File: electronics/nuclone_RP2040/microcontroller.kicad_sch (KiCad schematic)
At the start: 1 part

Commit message: WIP: added schematic component and started defining schematic
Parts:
- added U? (x3): (no value), symbol SquantorRaspberryPi:rp2040
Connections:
- net GPIO_00: now also U?.2 (GPIO0)
- net GPIO_01: now also U?.3 (GPIO1)
- net RESET: now also U?.26 (RUN)
- net TCK: now also U?.24 (SWCLK)
- net TMS: now also U?.25 (SWDIO)
- net VSS: now also U?.19 (TESTEN), U?.57 (GND)
- new net GPIO10: U?.13 (GPIO10)
- new net GPIO11: U?.14 (GPIO11)
- new net GPIO12: U?.15 (GPIO12)
- new net GPIO13: U?.16 (GPIO13)
- new net GPIO14: U?.17 (GPIO14)
- new net GPIO15: U?.18 (GPIO15)
- new net GPIO16: U?.27 (GPIO16)
- new net GPIO2: U?.4 (GPIO2)
- new net GPIO3: U?.5 (GPIO3)
- new net GPIO4: U?.6 (GPIO4)
- new net GPIO5: U?.7 (GPIO5)
- new net GPIO6: U?.8 (GPIO6)
- new net GPIO7: U?.9 (GPIO7)
- new net GPIO8: U?.11 (GPIO8)
- new net GPIO9: U?.12 (GPIO9)
- new net USB_DM: U?.46 (USB_DM)
- new net USB_DP: U?.47 (USB_DP)
- no-connect marks 30 -> 0

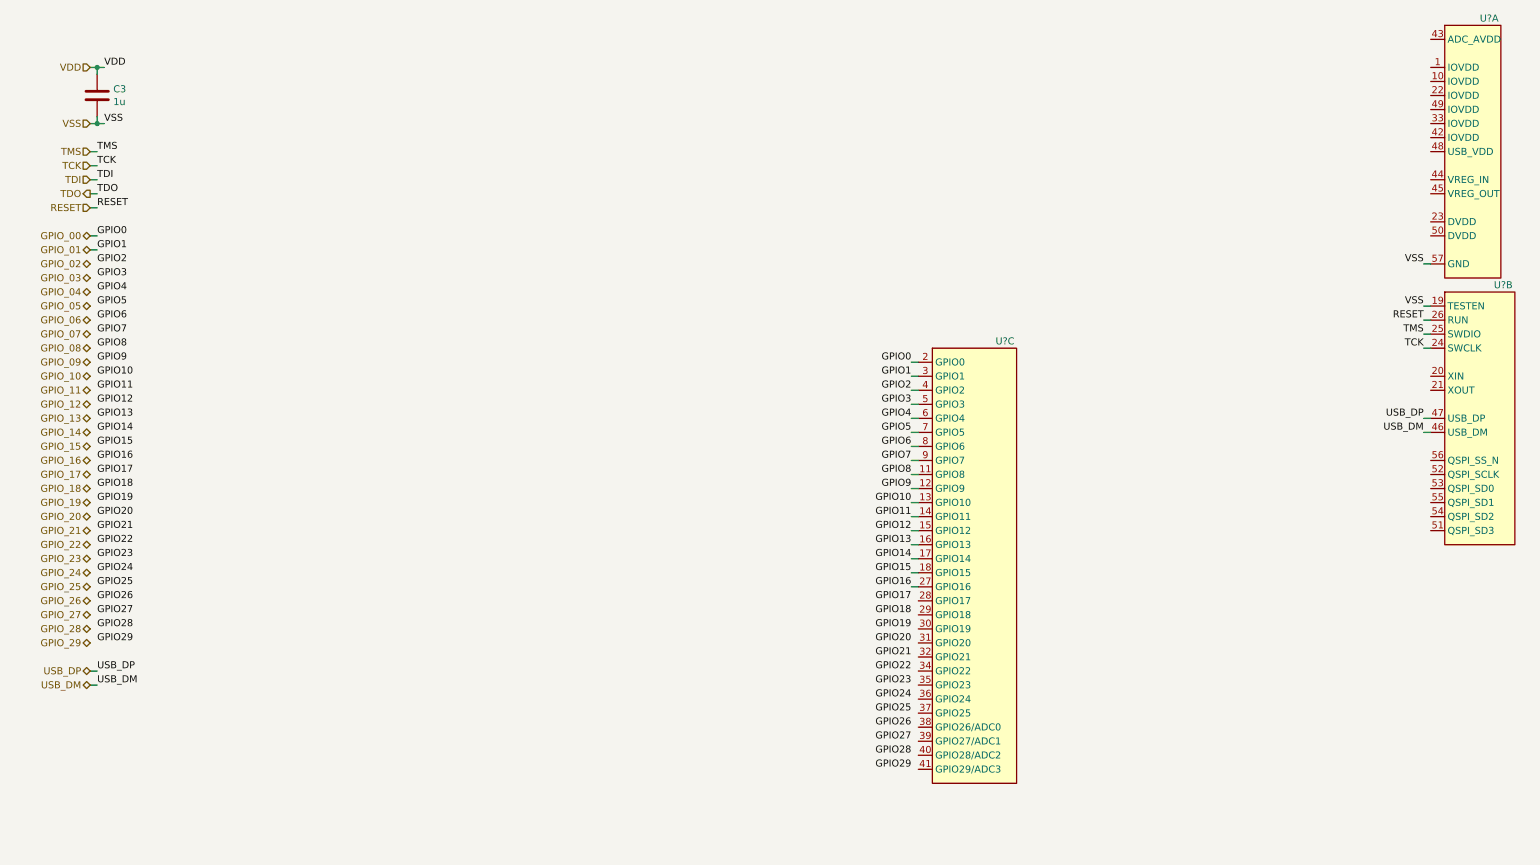
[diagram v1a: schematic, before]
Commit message: WIP rp2040 powersupply schematic part
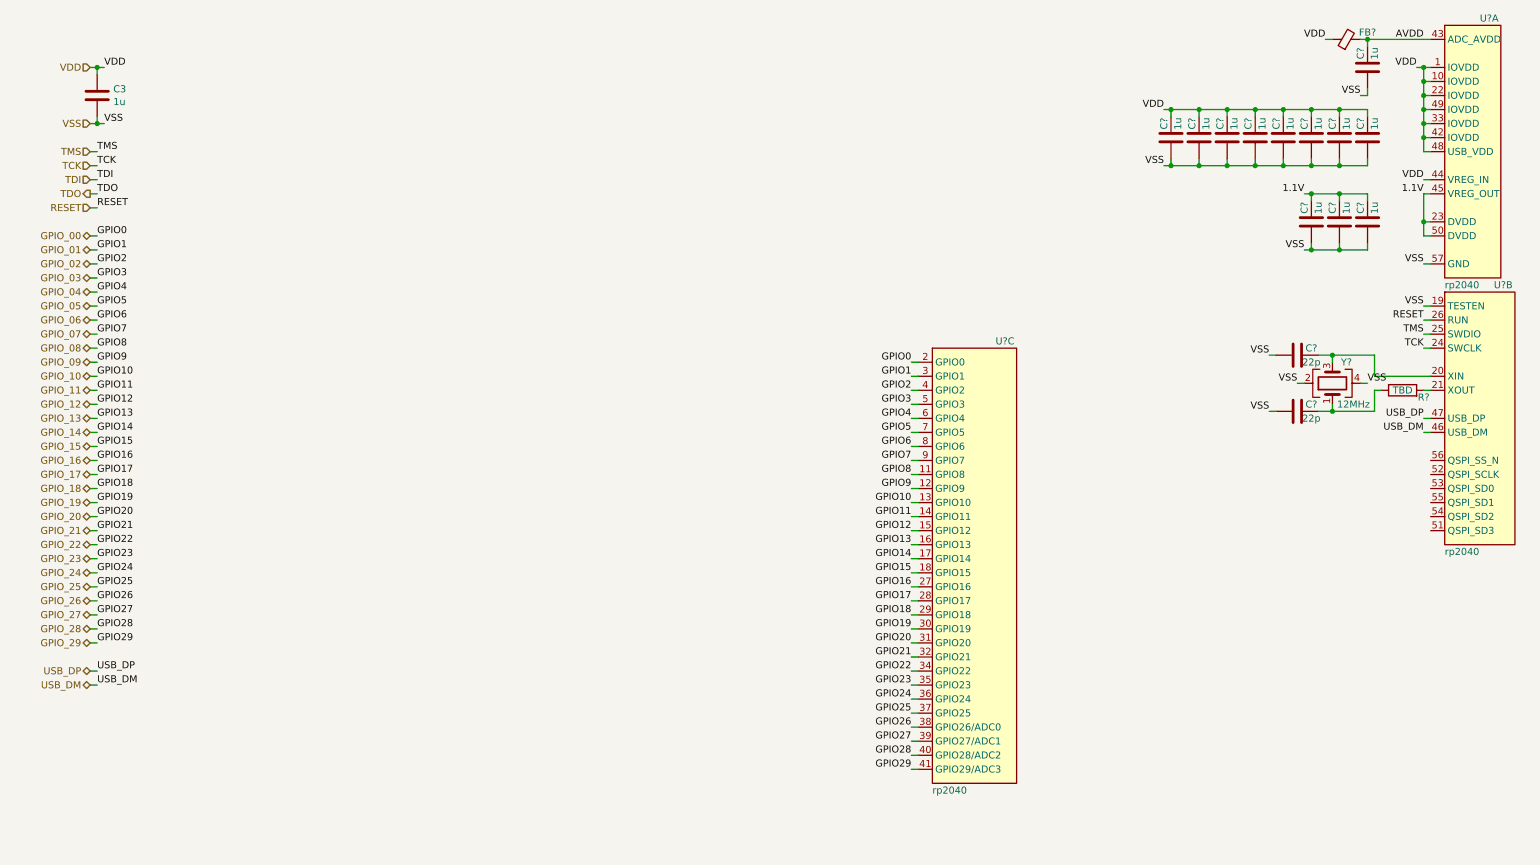
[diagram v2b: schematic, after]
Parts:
- added C? (x12): 1u, SquantorRcl:C_0402, symbol Device:C
- added C? (x2): 22p, SquantorRcl:C_0402, symbol Device:C
- added FB?: (no value), symbol Device:FerriteBead_Small
- added R?: TBD, SquantorRcl:R_0402_hand, symbol Device:R
- added Y?: 12MHz, SquantorCrystal:Crystal_3225_4, symbol Device:Crystal_GND24
- U? (x3): value (none) -> rp2040
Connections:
- net GPIO10 is gone; now on net GPIO_10: U?.13 (GPIO10)
- net GPIO11 is gone; now on net GPIO_11: U?.14 (GPIO11)
- net GPIO12 is gone; now on net GPIO_12: U?.15 (GPIO12)
- net GPIO13 is gone; now on net GPIO_13: U?.16 (GPIO13)
- net GPIO14 is gone; now on net GPIO_14: U?.17 (GPIO14)
- net GPIO15 is gone; now on net GPIO_15: U?.18 (GPIO15)
- net GPIO16 is gone; now on net GPIO_16: U?.27 (GPIO16)
- net GPIO2 is gone; now on net GPIO_02: U?.4 (GPIO2)
- net GPIO3 is gone; now on net GPIO_03: U?.5 (GPIO3)
- net GPIO4 is gone; now on net GPIO_04: U?.6 (GPIO4)
- net GPIO5 is gone; now on net GPIO_05: U?.7 (GPIO5)
- net GPIO6 is gone; now on net GPIO_06: U?.8 (GPIO6)
- net GPIO7 is gone; now on net GPIO_07: U?.9 (GPIO7)
- net GPIO8 is gone; now on net GPIO_08: U?.11 (GPIO8)
- net GPIO9 is gone; now on net GPIO_09: U?.12 (GPIO9)
- net GPIO_17: now also U?.28 (GPIO17)
- net GPIO_18: now also U?.29 (GPIO18)
- net GPIO_19: now also U?.30 (GPIO19)
- net GPIO_20: now also U?.31 (GPIO20)
- net GPIO_21: now also U?.32 (GPIO21)
- net GPIO_22: now also U?.34 (GPIO22)
- net GPIO_23: now also U?.35 (GPIO23)
- net GPIO_24: now also U?.36 (GPIO24)
- net GPIO_25: now also U?.37 (GPIO25)
- net GPIO_26: now also U?.38 (GPIO26/ADC0)
- net GPIO_27: now also U?.39 (GPIO27/ADC1)
- net GPIO_28: now also U?.40 (GPIO28/ADC2)
- net GPIO_29: now also U?.41 (GPIO29/ADC3)
- net VDD: now also U?.1 (IOVDD), U?.10 (IOVDD), U?.22 (IOVDD), U?.33 (IOVDD), U?.42 (IOVDD), U?.44 (VREG_IN), U?.48 (USB_VDD), U?.49 (IOVDD), C?.2, C?.2, C?.2, C?.2, C?.2, C?.2, C?.2, C?.2, FB?.1
- net VSS: now also C?.1, C?.1, C?.1, C?.1, C?.1, C?.1, C?.1, C?.1, C?.1, C?.1, C?.1, C?.1, C?.1, C?.1, Y?.2, Y?.4
- net at U?.20 (XIN): now also C?.2, Y?.3
- net at U?.21 (XOUT): now also R?.2
- net 1.1V: now reaches U?.23 (DVDD)
- net 1.1V: now also U?.45 (VREG_OUT), U?.50 (DVDD), C?.2, C?.2, C?.2
- net AVDD: now reaches U?.43 (ADC_AVDD)
- net AVDD: now also C?.2, FB?.2
- new net: C?.2, R?.1, Y?.1

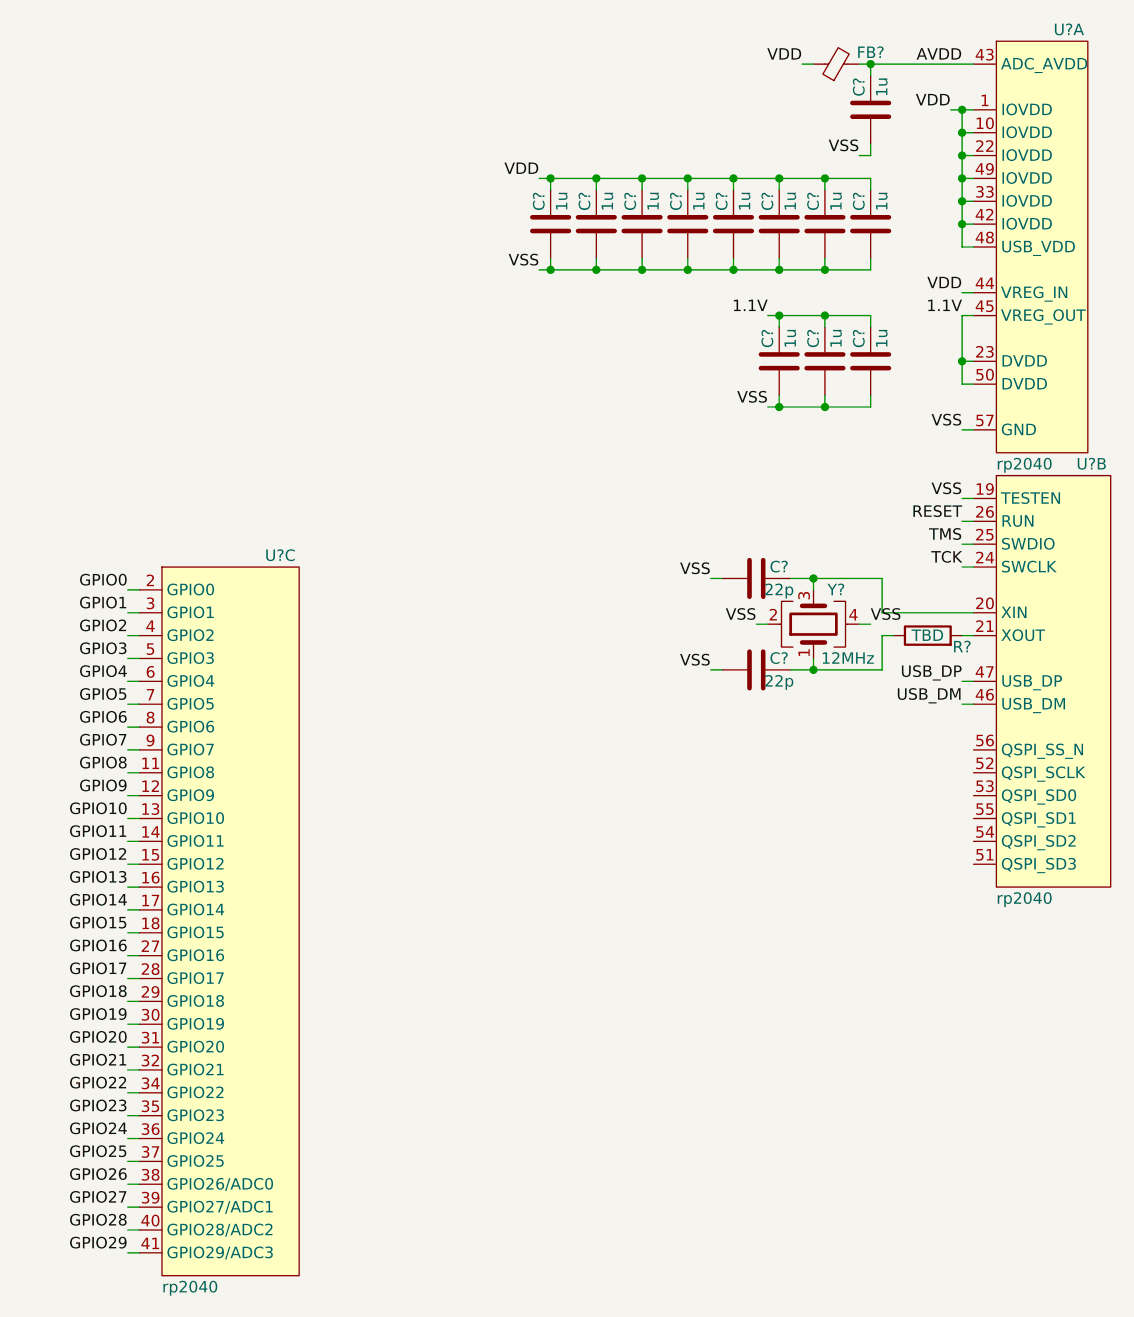
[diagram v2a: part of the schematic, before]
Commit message: updated missing footprint
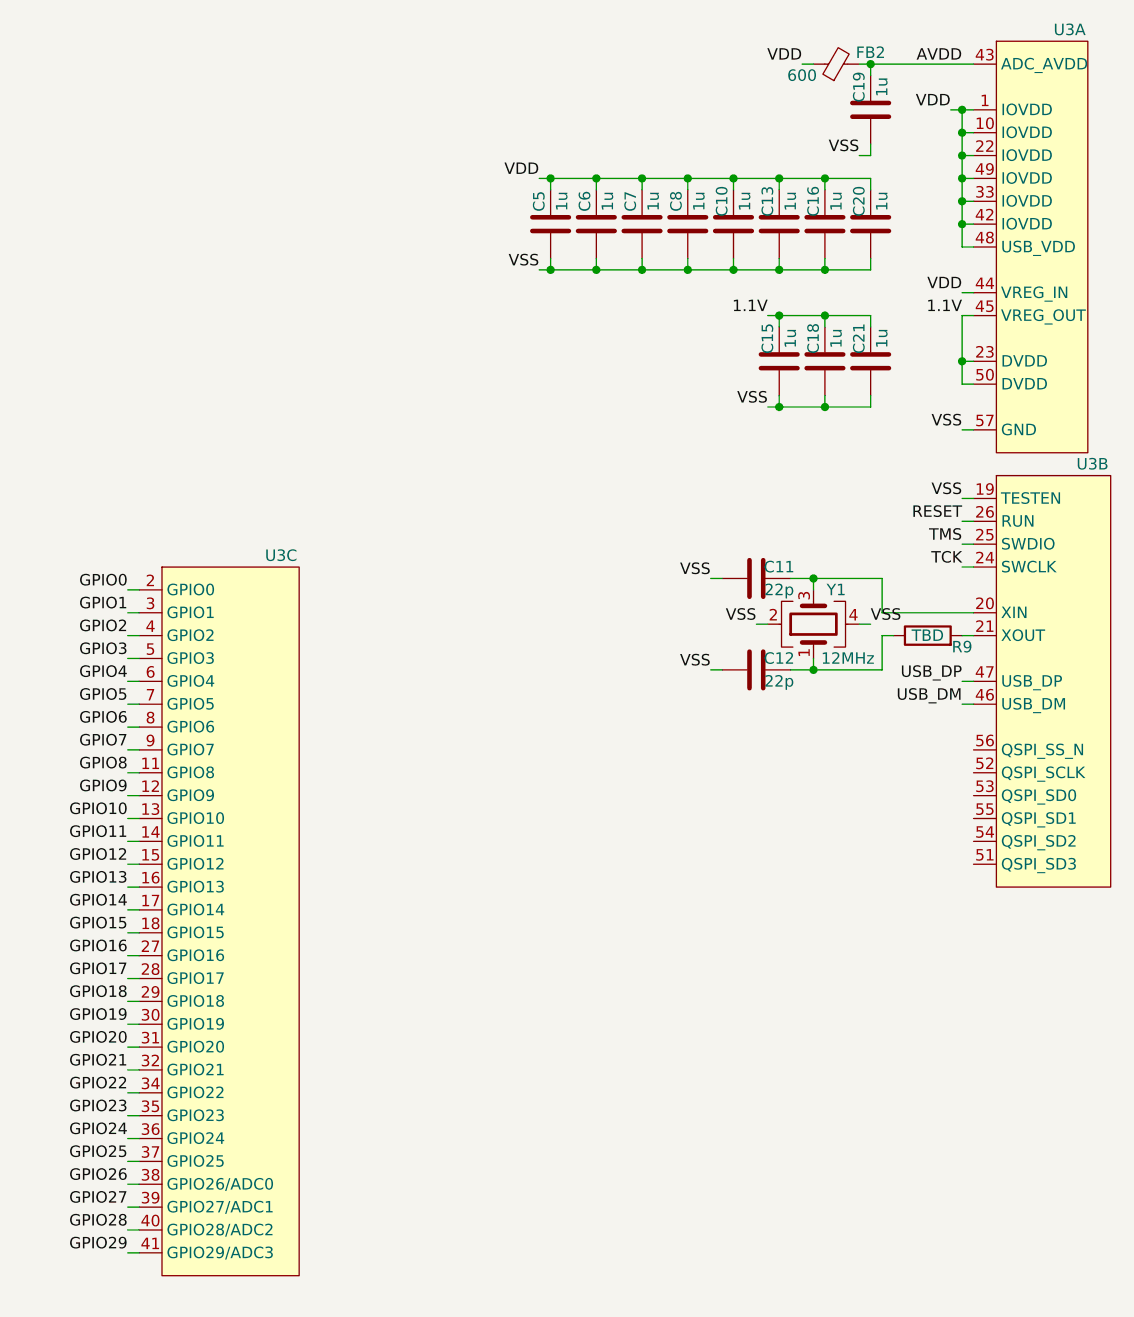
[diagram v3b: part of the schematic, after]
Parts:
- FB2: renamed from FB?; value (none) -> 600; footprint (none) -> SquantorRcl:L_0402
- U3: renamed from U?; value rp2040 -> (none)
- gave numbers to parts that had none: 16
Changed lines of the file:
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@@
   (symbol (lib_id "SquantorRaspberryPi:rp2040") (at 275.59 86.36 0) (unit 2)
     (in_bom yes) (on_board yes)
-    (property "Reference" "U?" (id 0) (at 278.13 62.23 0)
-      (effects (font (size 1.27 1.27)) (justify left))
-    )
-    (property "Value" "rp2040" (id 1) (at 269.24 110.49 0)
+    (property "Reference" "U3" (id 0) (at 278.13 62.23 0)
+      (effects (font (size 1.27 1.27)) (justify left))
+    )
+    (property "Value" "" (id 1) (at 269.24 110.49 0)
       (effects (font (size 1.27 1.27)) (justify left))
     )
@@
   (symbol (lib_id "Device:C") (at 255.27 50.8 180) (unit 1)
     (in_bom yes) (on_board yes)
-    (property "Reference" "C?" (id 0) (at 254 48.26 90))
+    (property "Reference" "C21" (id 0) (at 254 48.26 90))
     (property "Value" "1u" (id 1) (at 256.54 48.26 90))
     (property "Footprint" "SquantorRcl:C_0402" (id 2) (at 254.3048 46.99 0)
@@
   (symbol (lib_id "Device:R") (at 261.62 81.28 90) (unit 1)
     (in_bom yes) (on_board yes)
-    (property "Reference" "R?" (id 0) (at 265.43 82.55 90))
+    (property "Reference" "R9" (id 0) (at 265.43 82.55 90))
     (property "Value" "TBD" (id 1) (at 261.62 81.28 90))
     (property "Footprint" "SquantorRcl:R_0402_hand" (id 2) (at 261.62 83.058 90)
@@
   (symbol (lib_id "Device:C") (at 245.11 50.8 180) (unit 1)
     (in_bom yes) (on_board yes)
-    (property "Reference" "C?" (id 0) (at 243.84 48.26 90))
+    (property "Reference" "C15" (id 0) (at 243.84 48.26 90))
     (property "Value" "1u" (id 1) (at 246.38 48.26 90))
     (property "Footprint" "SquantorRcl:C_0402" (id 2) (at 244.1448 46.99 0)
@@
   (symbol (lib_id "SquantorRaspberryPi:rp2040") (at 274.32 38.1 0) (unit 1)
     (in_bom yes) (on_board yes)
-    (property "Reference" "U?" (id 0) (at 275.59 13.97 0)
-      (effects (font (size 1.27 1.27)) (justify left))
-    )
-    (property "Value" "rp2040" (id 1) (at 269.24 62.23 0)
+    (property "Reference" "U3" (id 0) (at 275.59 13.97 0)
+      (effects (font (size 1.27 1.27)) (justify left))
+    )
+    (property "Value" "" (id 1) (at 269.24 62.23 0)
       (effects (font (size 1.27 1.27)) (justify left))
     )
@@
   (symbol (lib_id "Device:C") (at 250.19 50.8 180) (unit 1)
     (in_bom yes) (on_board yes)
-    (property "Reference" "C?" (id 0) (at 248.92 48.26 90))
+    (property "Reference" "C18" (id 0) (at 248.92 48.26 90))
     (property "Value" "1u" (id 1) (at 251.46 48.26 90))
     (property "Footprint" "SquantorRcl:C_0402" (id 2) (at 249.2248 46.99 0)
@@
   (symbol (lib_id "Device:C") (at 229.87 35.56 180) (unit 1)
     (in_bom yes) (on_board yes)
-    (property "Reference" "C?" (id 0) (at 228.6 33.02 90))
+    (property "Reference" "C7" (id 0) (at 228.6 33.02 90))
     (property "Value" "1u" (id 1) (at 231.14 33.02 90))
     (property "Footprint" "SquantorRcl:C_0402" (id 2) (at 228.9048 31.75 0)
@@
   (symbol (lib_id "Device:C") (at 219.71 35.56 180) (unit 1)
     (in_bom yes) (on_board yes)
-    (property "Reference" "C?" (id 0) (at 218.44 33.02 90))
+    (property "Reference" "C5" (id 0) (at 218.44 33.02 90))
     (property "Value" "1u" (id 1) (at 220.98 33.02 90))
     (property "Footprint" "SquantorRcl:C_0402" (id 2) (at 218.7448 31.75 0)
@@
   (symbol (lib_id "Device:C") (at 250.19 35.56 180) (unit 1)
     (in_bom yes) (on_board yes)
-    (property "Reference" "C?" (id 0) (at 248.92 33.02 90))
+    (property "Reference" "C16" (id 0) (at 248.92 33.02 90))
     (property "Value" "1u" (id 1) (at 251.46 33.02 90))
     (property "Footprint" "SquantorRcl:C_0402" (id 2) (at 249.2248 31.75 0)
@@
   (symbol (lib_id "Device:Crystal_GND24") (at 248.92 80.01 90) (unit 1)
     (in_bom yes) (on_board yes)
-    (property "Reference" "Y?" (id 0) (at 251.46 76.2 90))
+    (property "Reference" "Y1" (id 0) (at 251.46 76.2 90))
     (property "Value" "12MHz" (id 1) (at 252.73 83.82 90))
     (property "Footprint" "SquantorCrystal:Crystal_3225_4" (id 2) (at 248.92 80.01 0)
@@
   (symbol (lib_id "Device:C") (at 245.11 35.56 180) (unit 1)
     (in_bom yes) (on_board yes)
-    (property "Reference" "C?" (id 0) (at 243.84 33.02 90))
+    (property "Reference" "C13" (id 0) (at 243.84 33.02 90))
     (property "Value" "1u" (id 1) (at 246.38 33.02 90))
     (property "Footprint" "SquantorRcl:C_0402" (id 2) (at 244.1448 31.75 0)
@@
   (symbol (lib_id "Device:C") (at 255.27 35.56 180) (unit 1)
     (in_bom yes) (on_board yes)
-    (property "Reference" "C?" (id 0) (at 254 33.02 90))
+    (property "Reference" "C20" (id 0) (at 254 33.02 90))
     (property "Value" "1u" (id 1) (at 256.54 33.02 90))
     (property "Footprint" "SquantorRcl:C_0402" (id 2) (at 254.3048 31.75 0)
@@
   (symbol (lib_id "Device:C") (at 234.95 35.56 180) (unit 1)
     (in_bom yes) (on_board yes)
-    (property "Reference" "C?" (id 0) (at 233.68 33.02 90))
+    (property "Reference" "C8" (id 0) (at 233.68 33.02 90))
     (property "Value" "1u" (id 1) (at 236.22 33.02 90))
     (property "Footprint" "SquantorRcl:C_0402" (id 2) (at 233.9848 31.75 0)
@@
   (symbol (lib_id "Device:C") (at 242.57 74.93 90) (unit 1)
     (in_bom yes) (on_board yes)
-    (property "Reference" "C?" (id 0) (at 245.11 73.66 90))
+    (property "Reference" "C11" (id 0) (at 245.11 73.66 90))
     (property "Value" "22p" (id 1) (at 245.11 76.2 90))
     (property "Footprint" "SquantorRcl:C_0402" (id 2) (at 246.38 73.9648 0)
@@
   (symbol (lib_id "Device:C") (at 224.79 35.56 180) (unit 1)
     (in_bom yes) (on_board yes)
-    (property "Reference" "C?" (id 0) (at 223.52 33.02 90))
+    (property "Reference" "C6" (id 0) (at 223.52 33.02 90))
     (property "Value" "1u" (id 1) (at 226.06 33.02 90))
     (property "Footprint" "SquantorRcl:C_0402" (id 2) (at 223.8248 31.75 0)
@@
   (symbol (lib_id "SquantorRaspberryPi:rp2040") (at 184.15 113.03 0) (unit 3)
     (in_bom yes) (on_board yes)
-    (property "Reference" "U?" (id 0) (at 187.96 72.39 0)
-      (effects (font (size 1.27 1.27)) (justify left))
-    )
-    (property "Value" "rp2040" (id 1) (at 176.53 153.67 0)
+    (property "Reference" "U3" (id 0) (at 187.96 72.39 0)
+      (effects (font (size 1.27 1.27)) (justify left))
+    )
+    (property "Value" "" (id 1) (at 176.53 153.67 0)
       (effects (font (size 1.27 1.27)) (justify left))
     )
@@
   (symbol (lib_id "Device:FerriteBead_Small") (at 251.46 17.78 90) (unit 1)
     (in_bom yes) (on_board yes)
-    (property "Reference" "FB?" (id 0) (at 255.27 16.51 90))
-    (property "Value" "" (id 1) (at 247.65 19.05 90))
-    (property "Footprint" "" (id 2) (at 251.46 19.558 90)
+    (property "Reference" "FB2" (id 0) (at 255.27 16.51 90))
+    (property "Value" "600" (id 1) (at 247.65 19.05 90))
+    (property "Footprint" "SquantorRcl:L_0402" (id 2) (at 251.46 19.558 90)
       (effects (font (size 1.27 1.27)) hide)
     )
@@
   (symbol (lib_id "Device:C") (at 240.03 35.56 180) (unit 1)
     (in_bom yes) (on_board yes)
-    (property "Reference" "C?" (id 0) (at 238.76 33.02 90))
+    (property "Reference" "C10" (id 0) (at 238.76 33.02 90))
     (property "Value" "1u" (id 1) (at 241.3 33.02 90))
     (property "Footprint" "SquantorRcl:C_0402" (id 2) (at 239.0648 31.75 0)
@@
   (symbol (lib_id "Device:C") (at 242.57 85.09 90) (unit 1)
     (in_bom yes) (on_board yes)
-    (property "Reference" "C?" (id 0) (at 245.11 83.82 90))
+    (property "Reference" "C12" (id 0) (at 245.11 83.82 90))
     (property "Value" "22p" (id 1) (at 245.11 86.36 90))
     (property "Footprint" "SquantorRcl:C_0402" (id 2) (at 246.38 84.1248 0)
@@
   (symbol (lib_id "Device:C") (at 255.27 22.86 180) (unit 1)
     (in_bom yes) (on_board yes)
-    (property "Reference" "C?" (id 0) (at 254 20.32 90))
+    (property "Reference" "C19" (id 0) (at 254 20.32 90))
     (property "Value" "1u" (id 1) (at 256.54 20.32 90))
     (property "Footprint" "SquantorRcl:C_0402" (id 2) (at 254.3048 19.05 0)
